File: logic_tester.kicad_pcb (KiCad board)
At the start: 2 copper layers, 36 parts, among them J1 15EDGR-3.5-02P, U1 LM339D, U2 LM317MDT

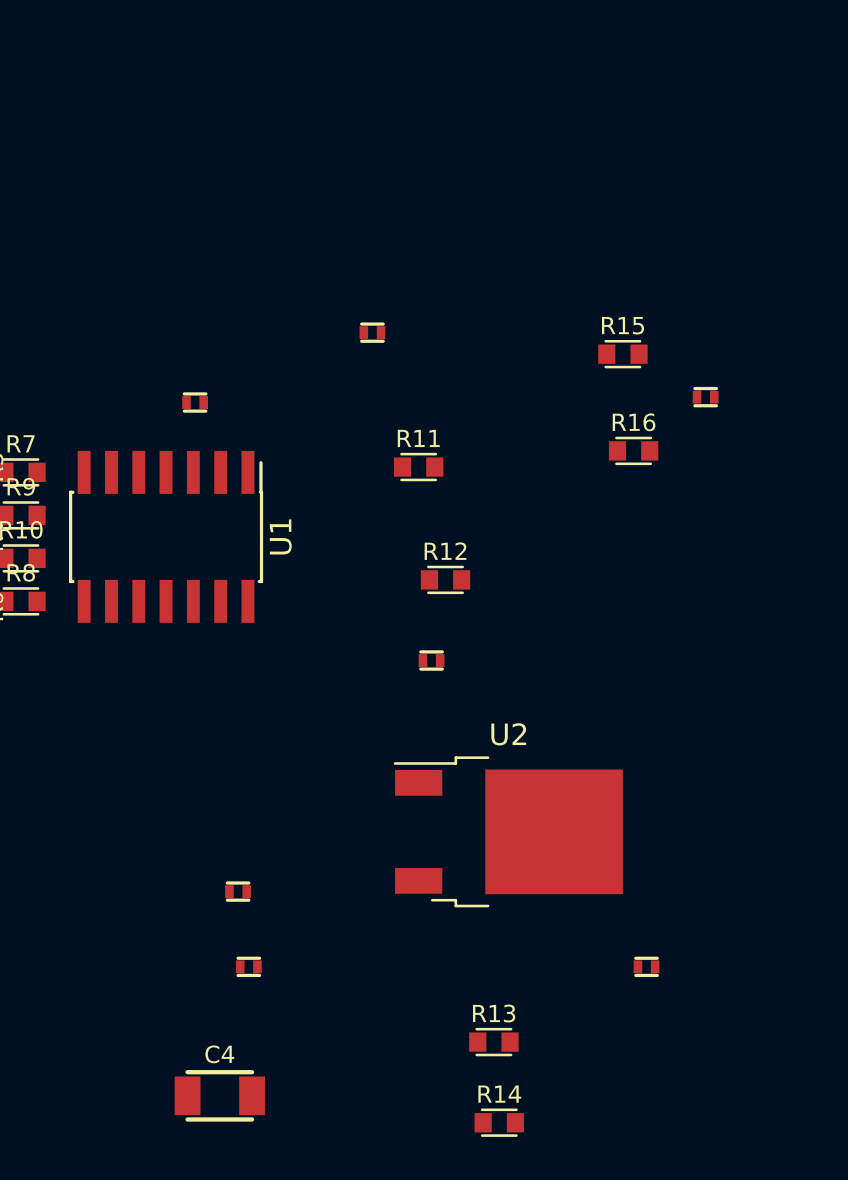
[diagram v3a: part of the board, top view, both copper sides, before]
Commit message: Second cascade of comparators placed
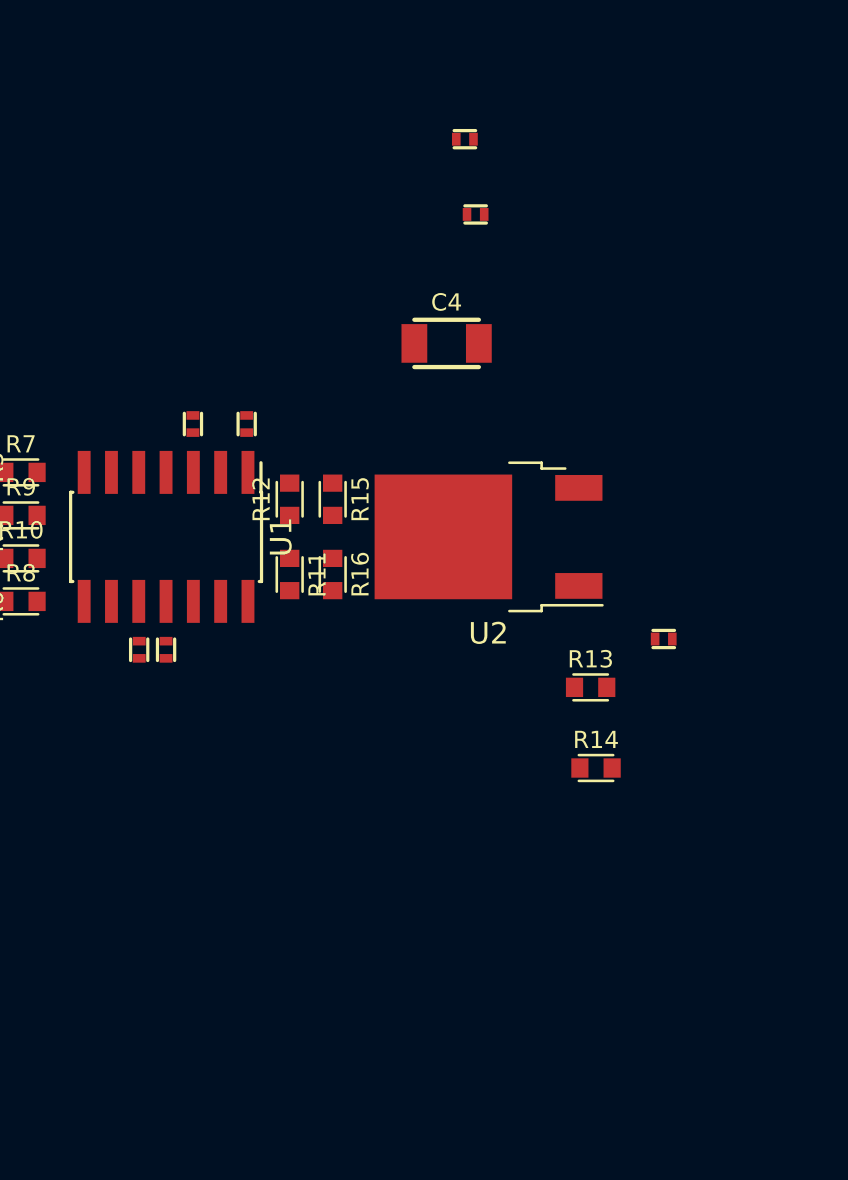
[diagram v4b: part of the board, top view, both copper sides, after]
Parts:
- moved C4 36.6 mm to (113.0, 91.0)
- moved C5 36.6 mm to (113.9, 81.5)
- moved C6 36.6 mm to (114.4, 85.0)
- moved C10 28.9 mm to (98.8, 105.2), turned to -90 degrees
- moved C7 17.6 mm to (100.0, 105.2), turned to -90 degrees
- moved R13 17.1 mm to (119.8, 107.0)
- moved R14 17.1 mm to (120.0, 110.8)
- moved C9 15.3 mm to (123.2, 104.8)
- moved R16 15.1 mm to (107.8, 101.8), turned to -90 degrees
- moved R15 15.1 mm to (107.8, 98.2), turned to -90 degrees
- moved C8 14.0 mm to (103.8, 94.8), turned to 90 degrees
- moved U2 13.8 mm to (115.0, 100.0), turned to 180 degrees
- moved R12 8.16 mm to (105.8, 98.2), turned to 90 degrees
- moved R11 7.81 mm to (105.8, 101.8), turned to -90 degrees
- moved C3 1.00 mm to (101.2, 94.8), turned to 90 degrees

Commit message: Seems fitted
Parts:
- moved D4 88.2 mm to (83.5, 103.2)
- moved D2 88.1 mm to (83.8, 96.8)
- moved R17 83.4 mm to (79.5, 97.2)
- moved R19 83.3 mm to (79.2, 102.8)
- moved D3 43.0 mm to (131.2, 102.0)
- moved R18 38.6 mm to (127.5, 102.0), turned to 90 degrees
- moved D1 35.0 mm to (130.2, 98.2)
- moved J1 24.5 mm to (138.0, 100.0)
- moved C5 19.5 mm to (125.8, 97.0), turned to 90 degrees
- moved C6 15.5 mm to (124.2, 97.0), turned to 90 degrees
- moved C4 15.3 mm to (125.0, 100.5), turned to -90 degrees
- moved R14 13.8 mm to (109.5, 101.8), turned to -90 degrees
- moved R13 13.5 mm to (109.5, 98.2), turned to -90 degrees
- moved C9 12.1 mm to (111.2, 102.5), turned to 180 degrees
- moved U2 2.80 mm to (117.8, 100.0)
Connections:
- J1 pad 1: Net-(D1-A) -> GNDD
- J1 pad 2: GNDD -> Net-(D1-A)

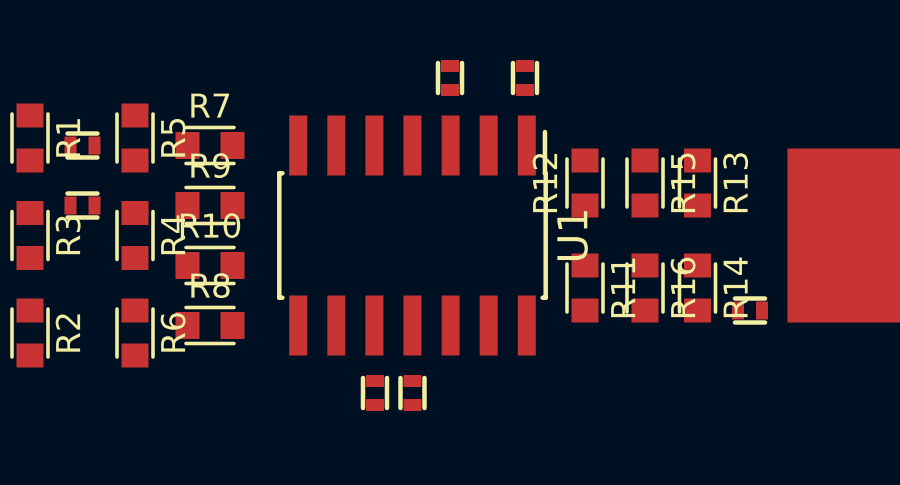
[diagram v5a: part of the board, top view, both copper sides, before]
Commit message: Tighter capacitor placement
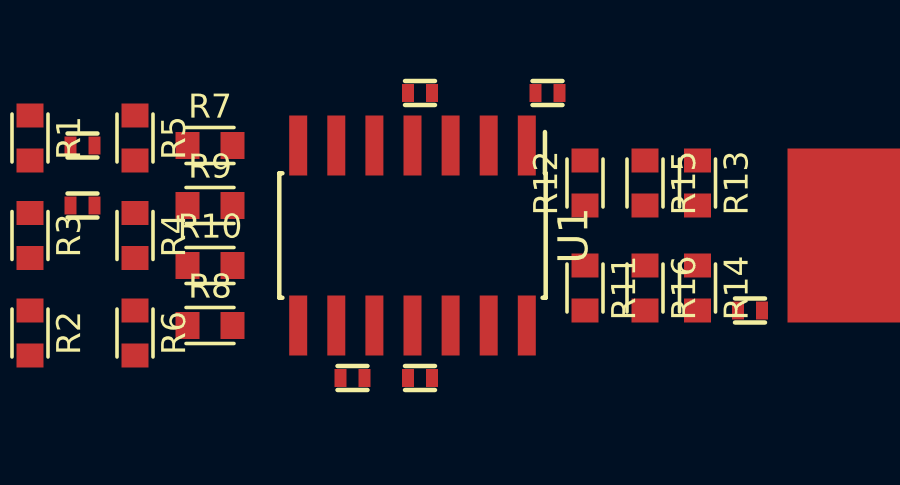
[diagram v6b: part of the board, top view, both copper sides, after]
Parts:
- moved C3 1.12 mm to (100.2, 95.2), turned to 180 degrees
- moved C10 0.90 mm to (98.0, 104.8), turned to 180 degrees
- moved C8 0.90 mm to (104.5, 95.2), turned to 0 degrees
- moved C7 0.56 mm to (100.2, 104.8), turned to 0 degrees
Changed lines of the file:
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@@
   )
   (footprint "NevaDA:C_0402" (layer "F.Cu")
-    (at 103.75 94.75 90)
+    (at 104.5 95.25)
     (descr "Capacitor SMD 0402")
     (tags "cap capacitor 0402")
@@
     (zone_connect 1)
     (attr smd)
-    (fp_text reference "C8" (at 0 -1.3 90) (layer "F.SilkS") hide
-        (effects (font (size 0.8 0.8) (thickness 0.15)))
-    )
-    (fp_text value "100n" (at 0 1.55 90) (layer "F.Fab") hide
-        (effects (font (size 1 1) (thickness 0.15)))
-    )
-    (fp_text user "${REFERENCE}" (at 0 0 90) (layer "F.Fab")
+    (fp_text reference "C8" (at 0 -1.3) (layer "F.SilkS") hide
+        (effects (font (size 0.8 0.8) (thickness 0.15)))
+    )
+    (fp_text value "100n" (at 0 1.55) (layer "F.Fab") hide
+        (effects (font (size 1 1) (thickness 0.15)))
+    )
+    (fp_text user "${REFERENCE}" (at 0 0) (layer "F.Fab")
         (effects (font (size 0.4 0.4) (thickness 0.1)))
     )
@@
     (fp_line (start -0.5 0.4) (end 0.5 0.4)
       (stroke (width 0.1) (type default)) (layer "F.Fab"))
-    (pad "1" smd rect (at -0.4 0 90) (size 0.4 0.6) (layers "F.Cu" "F.Paste" "F.Mask")
+    (pad "1" smd rect (at -0.4 0) (size 0.4 0.6) (layers "F.Cu" "F.Paste" "F.Mask")
       (net 1 "/CHK1") (pintype "passive"))
-    (pad "2" smd rect (at 0.4 0 90) (size 0.4 0.6) (layers "F.Cu" "F.Paste" "F.Mask")
+    (pad "2" smd rect (at 0.4 0) (size 0.4 0.6) (layers "F.Cu" "F.Paste" "F.Mask")
       (net 2 "GNDD") (pinfunction "GNDD") (pintype "power_in"))
     (model "${KISYS3DMOD}/Capacitor_SMD.3dshapes/C_0402_1005Metric.step"
@@
   )
   (footprint "NevaDA:C_0402" (layer "F.Cu")
-    (at 98.75 105.25 -90)
+    (at 98 104.75 180)
     (descr "Capacitor SMD 0402")
     (tags "cap capacitor 0402")
@@
     (zone_connect 1)
     (attr smd)
-    (fp_text reference "C10" (at 0 -1.3 90) (layer "F.SilkS") hide
-        (effects (font (size 0.8 0.8) (thickness 0.15)))
-    )
-    (fp_text value "100n" (at 0 1.55 90) (layer "F.Fab") hide
-        (effects (font (size 1 1) (thickness 0.15)))
-    )
-    (fp_text user "${REFERENCE}" (at 0 0 90) (layer "F.Fab")
+    (fp_text reference "C10" (at 0 -1.3) (layer "F.SilkS") hide
+        (effects (font (size 0.8 0.8) (thickness 0.15)))
+    )
+    (fp_text value "100n" (at 0 1.55) (layer "F.Fab") hide
+        (effects (font (size 1 1) (thickness 0.15)))
+    )
+    (fp_text user "${REFERENCE}" (at 0 0) (layer "F.Fab")
         (effects (font (size 0.4 0.4) (thickness 0.1)))
     )
@@
     (fp_line (start -0.5 0.4) (end 0.5 0.4)
       (stroke (width 0.1) (type default)) (layer "F.Fab"))
-    (pad "1" smd rect (at -0.4 0 270) (size 0.4 0.6) (layers "F.Cu" "F.Paste" "F.Mask")
+    (pad "1" smd rect (at -0.4 0 180) (size 0.4 0.6) (layers "F.Cu" "F.Paste" "F.Mask")
       (net 3 "/REF_D") (pintype "passive"))
-    (pad "2" smd rect (at 0.4 0 270) (size 0.4 0.6) (layers "F.Cu" "F.Paste" "F.Mask")
+    (pad "2" smd rect (at 0.4 0 180) (size 0.4 0.6) (layers "F.Cu" "F.Paste" "F.Mask")
       (net 2 "GNDD") (pinfunction "GNDD") (pintype "power_in"))
     (model "${KISYS3DMOD}/Capacitor_SMD.3dshapes/C_0402_1005Metric.step"
@@
   )
   (footprint "NevaDA:C_0402" (layer "F.Cu")
-    (at 100 105.25 -90)
+    (at 100.25 104.75)
     (descr "Capacitor SMD 0402")
     (tags "cap capacitor 0402")
@@
     (zone_connect 1)
     (attr smd)
-    (fp_text reference "C7" (at 0 -1.3 90) (layer "F.SilkS") hide
-        (effects (font (size 0.8 0.8) (thickness 0.15)))
-    )
-    (fp_text value "100n" (at 0 1.55 90) (layer "F.Fab") hide
-        (effects (font (size 1 1) (thickness 0.15)))
-    )
-    (fp_text user "${REFERENCE}" (at 0 0 90) (layer "F.Fab")
+    (fp_text reference "C7" (at 0 -1.3) (layer "F.SilkS") hide
+        (effects (font (size 0.8 0.8) (thickness 0.15)))
+    )
+    (fp_text value "100n" (at 0 1.55) (layer "F.Fab") hide
+        (effects (font (size 1 1) (thickness 0.15)))
+    )
+    (fp_text user "${REFERENCE}" (at 0 0) (layer "F.Fab")
         (effects (font (size 0.4 0.4) (thickness 0.1)))
     )
@@
     (fp_line (start -0.5 0.4) (end 0.5 0.4)
       (stroke (width 0.1) (type default)) (layer "F.Fab"))
-    (pad "1" smd rect (at -0.4 0 270) (size 0.4 0.6) (layers "F.Cu" "F.Paste" "F.Mask")
+    (pad "1" smd rect (at -0.4 0) (size 0.4 0.6) (layers "F.Cu" "F.Paste" "F.Mask")
       (net 4 "/CHK0") (pintype "passive"))
-    (pad "2" smd rect (at 0.4 0 270) (size 0.4 0.6) (layers "F.Cu" "F.Paste" "F.Mask")
+    (pad "2" smd rect (at 0.4 0) (size 0.4 0.6) (layers "F.Cu" "F.Paste" "F.Mask")
       (net 2 "GNDD") (pinfunction "GNDD") (pintype "power_in"))
     (model "${KISYS3DMOD}/Capacitor_SMD.3dshapes/C_0402_1005Metric.step"
@@
   )
   (footprint "NevaDA:C_0402" (layer "F.Cu")
-    (at 101.25 94.75 90)
+    (at 100.25 95.25 180)
     (descr "Capacitor SMD 0402")
     (tags "cap capacitor 0402")
@@
     (zone_connect 1)
     (attr smd)
-    (fp_text reference "C3" (at 0 -1.3 90) (layer "F.SilkS") hide
-        (effects (font (size 0.8 0.8) (thickness 0.15)))
-    )
-    (fp_text value "100n" (at 0 1.55 90) (layer "F.Fab") hide
-        (effects (font (size 1 1) (thickness 0.15)))
-    )
-    (fp_text user "${REFERENCE}" (at 0 0 90) (layer "F.Fab")
+    (fp_text reference "C3" (at 0 -1.3) (layer "F.SilkS") hide
+        (effects (font (size 0.8 0.8) (thickness 0.15)))
+    )
+    (fp_text value "100n" (at 0 1.55) (layer "F.Fab") hide
+        (effects (font (size 1 1) (thickness 0.15)))
+    )
+    (fp_text user "${REFERENCE}" (at 0 0) (layer "F.Fab")
         (effects (font (size 0.4 0.4) (thickness 0.1)))
     )
@@
     (fp_line (start -0.5 0.4) (end 0.5 0.4)
       (stroke (width 0.1) (type default)) (layer "F.Fab"))
-    (pad "1" smd rect (at -0.4 0 90) (size 0.4 0.6) (layers "F.Cu" "F.Paste" "F.Mask")
+    (pad "1" smd rect (at -0.4 0 180) (size 0.4 0.6) (layers "F.Cu" "F.Paste" "F.Mask")
       (net 7 "V+") (pintype "passive"))
-    (pad "2" smd rect (at 0.4 0 90) (size 0.4 0.6) (layers "F.Cu" "F.Paste" "F.Mask")
+    (pad "2" smd rect (at 0.4 0 180) (size 0.4 0.6) (layers "F.Cu" "F.Paste" "F.Mask")
       (net 2 "GNDD") (pinfunction "GNDD") (pintype "power_in"))
     (model "${KISYS3DMOD}/Capacitor_SMD.3dshapes/C_0402_1005Metric.step"

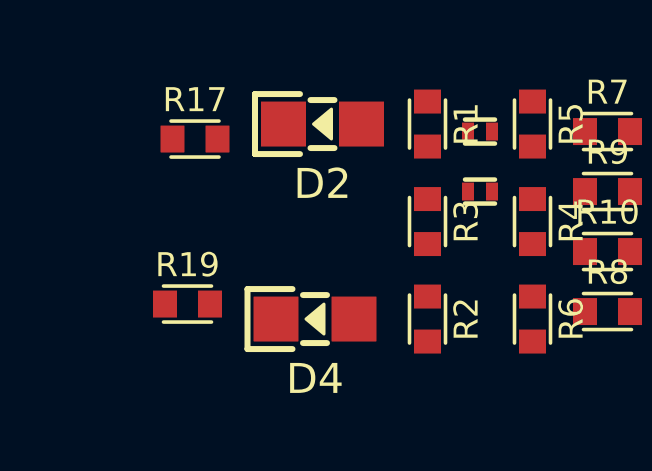
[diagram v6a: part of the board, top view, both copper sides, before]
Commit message: Probe pad added
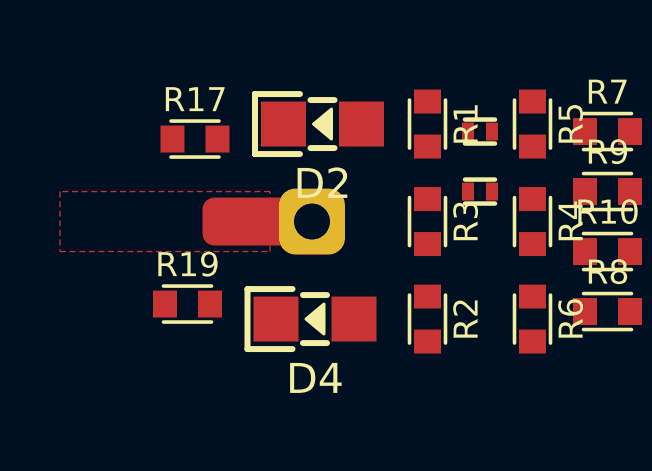
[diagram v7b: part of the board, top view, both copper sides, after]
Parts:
- added J2: Probe, NevaDA:Pad_Wire, F.Cu at (83.4, 100.0)
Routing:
- added copper zone on F.Cu, net /PROBE
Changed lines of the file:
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@@
     )
+  )
+  (footprint "NevaDA:Pad_Wire" (layer "F.Cu")
+    (at 83.4 100 180)
+    (property "Ceramic" "")
+    (property "Role" "")
+    (property "Sheetfile" "logic_tester.kicad_sch")
+    (property "Sheetname" "")
+    (property "Vcc" "")
+    (property "Voltage" "")
+    (property "ki_description" "Generic connector, single row, 01x01, script generated")
+    (property "ki_keywords" "connector")
+    (attr through_hole)
+    (fp_text reference "J2" (at -1.5 0) (layer "F.SilkS") hide
+        (effects (font (size 1 1) (thickness 0.15)) (justify left))
+    )
+    (fp_text value "Probe" (at 0 0) (layer "F.Fab") hide
+        (effects (font (size 1 1) (thickness 0.15)))
+    )
+    (fp_line (start -1.25 -1.25) (end -1.25 1.25)
+      (stroke (width 0.12) (type solid)) (layer "B.CrtYd"))
+    (fp_line (start -1.25 1.25) (end 1.25 1.25)
+      (stroke (width 0.12) (type solid)) (layer "B.CrtYd"))
+    (fp_line (start 1.25 -1.25) (end -1.25 -1.25)
+      (stroke (width 0.12) (type solid)) (layer "B.CrtYd"))
+    (fp_line (start 1.25 1.25) (end 1.25 -1.25)
+      (stroke (width 0.12) (type solid)) (layer "B.CrtYd"))
+    (fp_line (start -1.25 -1.25) (end -1.25 1.25)
+      (stroke (width 0.12) (type solid)) (layer "F.CrtYd"))
+    (fp_line (start -1.25 1.25) (end 4 1.25)
+      (stroke (width 0.12) (type solid)) (layer "F.CrtYd"))
+    (fp_line (start 4 -1.25) (end -1.25 -1.25)
+      (stroke (width 0.12) (type solid)) (layer "F.CrtYd"))
+    (fp_line (start 4 1.25) (end 4 -1.25)
+      (stroke (width 0.12) (type solid)) (layer "F.CrtYd"))
+    (pad "1" thru_hole roundrect (at 0 0 180) (size 2.2 2.2) (drill 1.2) (layers "*.Cu" "*.Mask") (roundrect_rratio 0.25)
+      (net 13 "/PROBE") (pinfunction "Pin_1") (pintype "passive"))
+    (pad "1" smd roundrect (at 1.4 0 180) (size 4.5 1.6) (layers "F.Cu" "F.Mask") (roundrect_rratio 0.25)
+      (net 13 "/PROBE") (pinfunction "Pin_1") (pintype "passive"))
   )
   (footprint "NevaDA:R_0603" (layer "F.Cu")
@@
     )
   )
+  (gr_line (start 81 106) (end 111 106)
+    (stroke (width 0.1) (type default)) (layer "Margin"))
+  (gr_line (start 75 103) (end 81 106)
+    (stroke (width 0.1) (type default)) (layer "Margin"))
+  (gr_line (start 111 106) (end 112 105)
+    (stroke (width 0.1) (type default)) (layer "Margin"))
+  (gr_line (start 112 95) (end 111 94)
+    (stroke (width 0.1) (type default)) (layer "Margin"))
+  (gr_line (start 75 97) (end 75 103)
+    (stroke (width 0.1) (type default)) (layer "Margin"))
+  (gr_line (start 112 105) (end 117 105)
+    (stroke (width 0.1) (type default)) (layer "Margin"))
+  (gr_line (start 117 95) (end 112 95)
+    (stroke (width 0.1) (type default)) (layer "Margin"))
+  (gr_line (start 143 106) (end 143 94)
+    (stroke (width 0.1) (type default)) (layer "Margin"))
+  (gr_line (start 118 94) (end 117 95)
+    (stroke (width 0.1) (type default)) (layer "Margin"))
+  (gr_line (start 143 94) (end 118 94)
+    (stroke (width 0.1) (type default)) (layer "Margin"))
+  (gr_line (start 117 105) (end 118 106)
+    (stroke (width 0.1) (type default)) (layer "Margin"))
+  (gr_line (start 118 106) (end 143 106)
+    (stroke (width 0.1) (type default)) (layer "Margin"))
+  (gr_line (start 111 94) (end 81 94)
+    (stroke (width 0.1) (type default)) (layer "Margin"))
+  (gr_line (start 75 97) (end 81 94)
+    (stroke (width 0.1) (type default)) (layer "Margin"))
+  (zone (net 13) (net_name "/PROBE") (layer "F.Cu") (name "PROBE") (hatch edge 0.5)
+    (priority 30)
+    (connect_pads yes (clearance 0.5))
+    (min_thickness 0.25) (filled_areas_thickness no)
+    (fill yes (thermal_gap 0.5) (thermal_bridge_width 0.5) (smoothing fillet) (radius 1))
+    (polygon
+      (pts
+        (xy 75 99)
+        (xy 75 101)
+        (xy 82 101)
+        (xy 82 99)
+      )
+    )
+  )

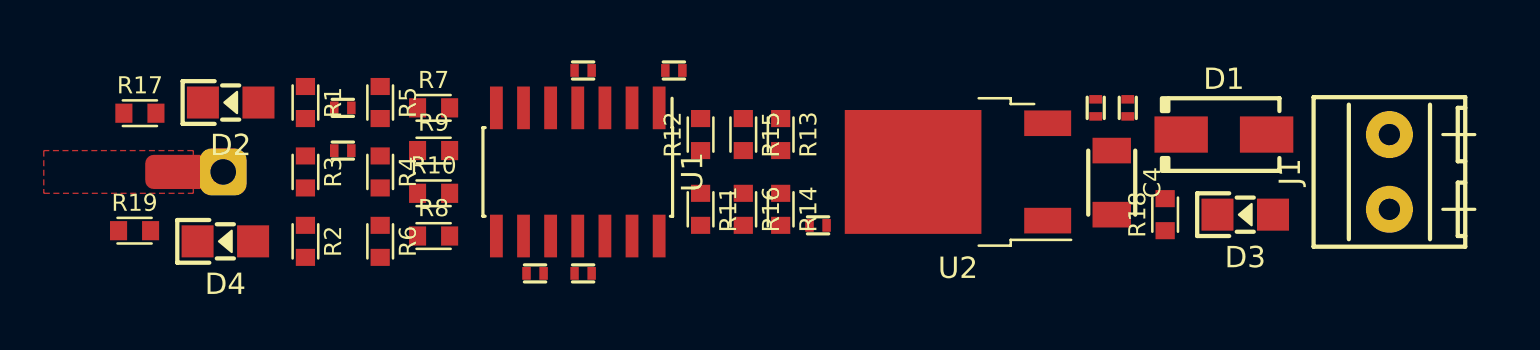
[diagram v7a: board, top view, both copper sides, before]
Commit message: Signal part routed
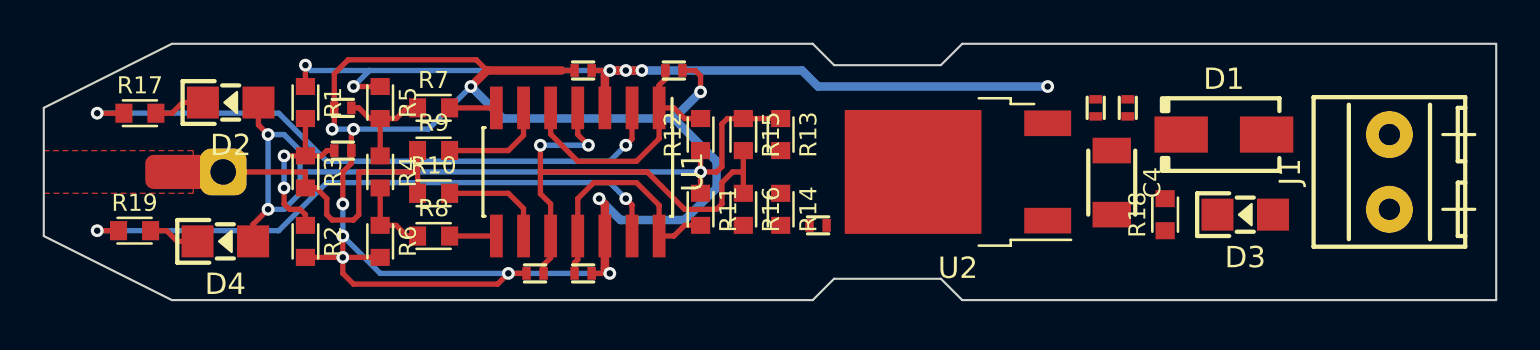
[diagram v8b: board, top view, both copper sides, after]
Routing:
- net GNDD: track 0.00 -> 84.2 mm, vias 0 -> 10
- net V+: track 0.00 -> 42.7 mm, vias 0 -> 6
- net /VCC_REG: track 0.00 -> 39.3 mm, vias 0 -> 3
- net Net-(R17-Pad1): track 0.00 -> 29.1 mm, vias 0 -> 2
- net Net-(R19-Pad1): track 0.00 -> 28.9 mm, vias 0 -> 2
- net /REF_D: track 0.00 -> 24.1 mm, vias 0 -> 2
- net /PROBE: track 0.00 -> 15.0 mm
- net /CHK1: track 0.00 -> 12.7 mm
- net /CHK0: track 0.00 -> 11.7 mm
- net /CENTER: track 0.00 -> 8.16 mm, vias 0 -> 2
- net /REF1: track 0.00 -> 5.26 mm
- net Net-(U1D-+): track 0.00 -> 5.04 mm
- net Net-(U1B--): track 0.00 -> 5.04 mm
- net /REF0: track 0.00 -> 3.71 mm
- net Net-(D4-K): track 0.00 -> 2.41 mm
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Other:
- board outline added: 68 x 12 mm
